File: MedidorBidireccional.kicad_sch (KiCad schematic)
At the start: 28 parts, among them J1 ADC conector, J2 Pickit, U1 RN4870-I_RM140, U2 47L04-E_ST, U3 25AA320A-I_ST, U4 PIC24FJ128GA310-I_PT

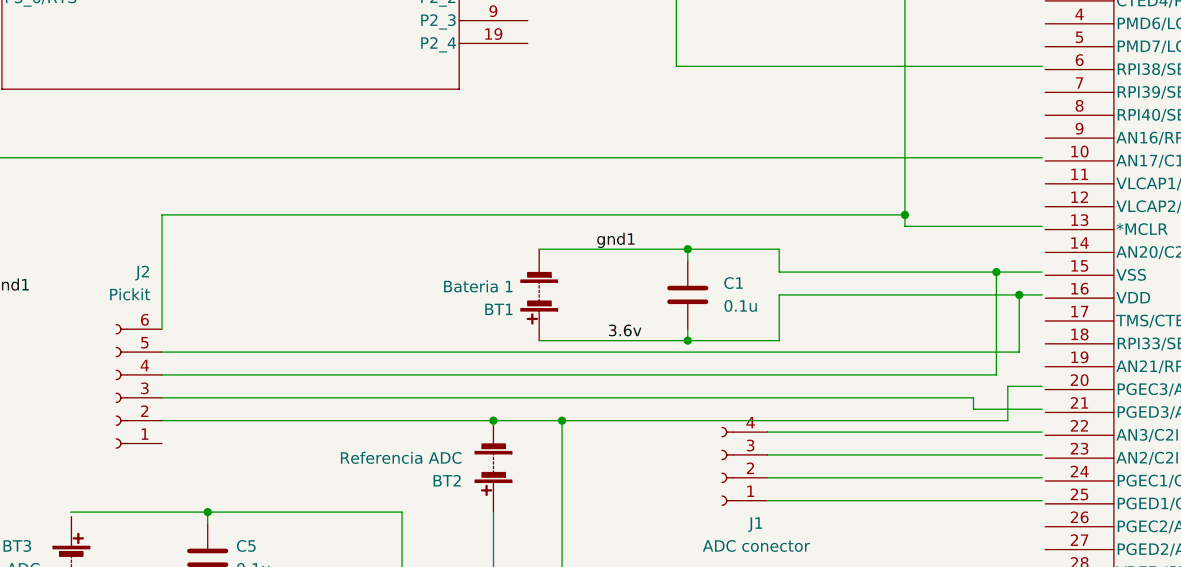
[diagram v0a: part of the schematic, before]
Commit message: se añade resistencia para pickit
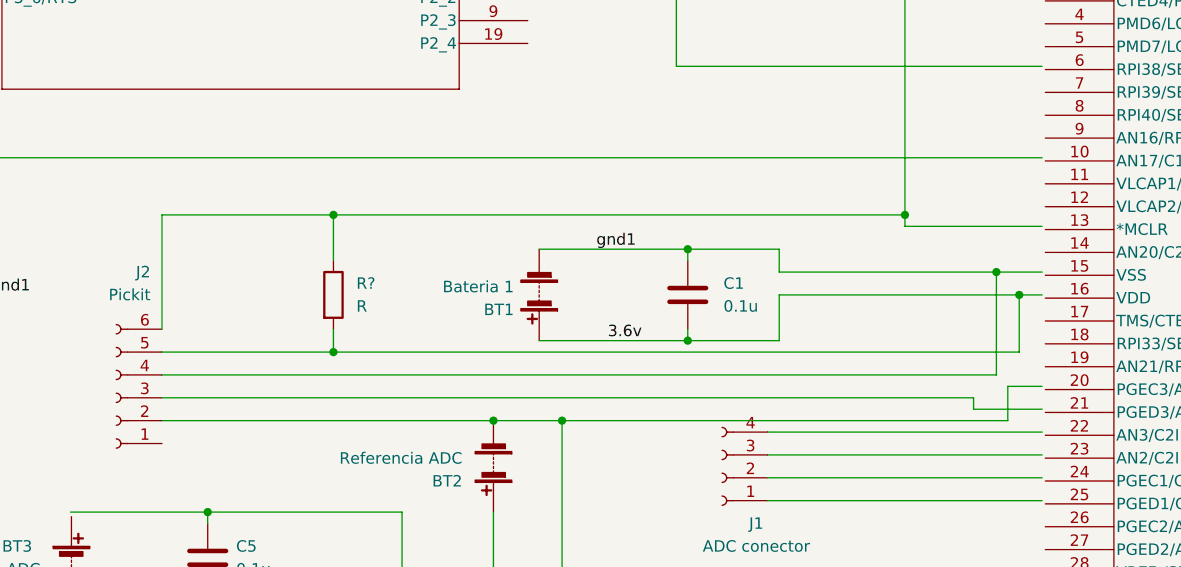
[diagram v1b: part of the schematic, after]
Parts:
- added R?: R, symbol Device:R
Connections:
- net 3.6v: now also R?.2
- net at J2.6 (Pin_6), R2.1: now also R?.1
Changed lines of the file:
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@@
   (junction (at 201.93 254) (diameter 0) (color 0 0 0 0)
   )
+  (junction (at 144.78 162.56) (diameter 0) (color 0 0 0 0)
+  )
   (junction (at 208.28 162.56) (diameter 0) (color 0 0 0 0)
   )
@@
   )
   (junction (at 198.12 226.06) (diameter 0) (color 0 0 0 0)
+  )
+  (junction (at 144.78 177.8) (diameter 0) (color 0 0 0 0)
   )
   (junction (at 170.18 185.42) (diameter 0) (color 0 0 0 0)
@@
     (stroke (width 0) (type default) (color 0 0 0 0))
   )
+  (wire (pts (xy 144.78 177.8) (xy 220.98 177.8))
+    (stroke (width 0) (type default) (color 0 0 0 0))
+  )
   (wire (pts (xy 467.36 82.55) (xy 538.48 82.55))
     (stroke (width 0) (type default) (color 0 0 0 0))
@@
     (stroke (width 0) (type default) (color 0 0 0 0))
   )
+  (wire (pts (xy 144.78 175.26) (xy 144.78 177.8))
+    (stroke (width 0) (type default) (color 0 0 0 0))
+  )
   (wire (pts (xy 220.98 171.45) (xy 223.52 171.45))
     (stroke (width 0) (type default) (color 0 0 0 0))
@@
     (stroke (width 0) (type default) (color 0 0 0 0))
   )
-  (wire (pts (xy 125.73 162.56) (xy 208.28 162.56))
+  (wire (pts (xy 125.73 162.56) (xy 144.78 162.56))
     (stroke (width 0) (type default) (color 0 0 0 0))
   )
@@
     (stroke (width 0) (type default) (color 0 0 0 0))
   )
-  (wire (pts (xy 125.73 177.8) (xy 220.98 177.8))
+  (wire (pts (xy 125.73 177.8) (xy 144.78 177.8))
     (stroke (width 0) (type default) (color 0 0 0 0))
   )
@@
     (stroke (width 0) (type default) (color 0 0 0 0))
   )
+  (wire (pts (xy 144.78 162.56) (xy 208.28 162.56))
+    (stroke (width 0) (type default) (color 0 0 0 0))
+  )
   (wire (pts (xy 480.06 97.79) (xy 525.78 97.79))
     (stroke (width 0) (type default) (color 0 0 0 0))
@@
   )
   (wire (pts (xy 431.8 194.31) (xy 482.6 194.31))
+    (stroke (width 0) (type default) (color 0 0 0 0))
+  )
+  (wire (pts (xy 144.78 162.56) (xy 144.78 167.64))
     (stroke (width 0) (type default) (color 0 0 0 0))
   )
@@
     (pin "9")
   )
+  (symbol (lib_id "Device:R") (at 144.78 171.45 0) (unit 1)
+    (in_bom yes) (on_board yes) (fields_autoplaced)
+    (property "Reference" "R?" (id 0) (at 147.32 170.1799 0)
+      (effects (font (size 1.27 1.27)) (justify left))
+    )
+    (property "Value" "R" (id 1) (at 147.32 172.7199 0)
+      (effects (font (size 1.27 1.27)) (justify left))
+    )
+    (property "Footprint" "" (id 2) (at 143.002 171.45 90)
+      (effects (font (size 1.27 1.27)) hide)
+    )
+    (property "Datasheet" "~" (id 3) (at 144.78 171.45 0)
+      (effects (font (size 1.27 1.27)) hide)
+    )
+    (pin "1")
+    (pin "2")
+  )
   (symbol (lib_id "Connector:Conn_01x18_Female") (at 523.24 120.65 90) (unit 1)
     (in_bom yes) (on_board yes)
@@
       (reference "R6") (unit 1) (value "330") (footprint "")
     )
+    (path "/7cf4a546-1a3b-444f-85e5-1343f72e38f0"
+      (reference "R?") (unit 1) (value "R") (footprint "")
+    )
     (path "/9b2818c2-72ef-4d3f-9cc7-e18b19154a65"

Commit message: se actualiza circuito de conector de pickit
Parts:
- added C10: 10uF, symbol Device:C
- added J3, J4: Jp, symbol Connector:Conn_01x01_Female
- C6: value C -> 6.8uF
- R7: renamed from R?; value R -> 10K
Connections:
- net gnd1: now also C10.2
- net at J2.6 (Pin_6), R7.1: now also J4.1 (Pin_1); no longer R2.1
- new net: J3.1 (Pin_1), R2.1
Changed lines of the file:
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@@
   (junction (at 201.93 254) (diameter 0) (color 0 0 0 0)
   )
+  (junction (at 208.28 162.56) (diameter 0) (color 0 0 0 0)
+  )
   (junction (at 144.78 162.56) (diameter 0) (color 0 0 0 0)
   )
-  (junction (at 208.28 162.56) (diameter 0) (color 0 0 0 0)
-  )
   (junction (at 35.56 120.65) (diameter 0) (color 0 0 0 0)
   )
@@
   )
   (junction (at 130.81 205.74) (diameter 0) (color 0 0 0 0)
+  )
+  (junction (at 494.03 196.85) (diameter 0) (color 0 0 0 0)
   )
   (no_connect (at 515.62 110.49))
@@
     (stroke (width 0) (type default) (color 0 0 0 0))
   )
+  (wire (pts (xy 494.03 182.88) (xy 494.03 196.85))
+    (stroke (width 0) (type default) (color 0 0 0 0))
+  )
   (wire (pts (xy 535.94 125.73) (xy 535.94 158.75))
     (stroke (width 0) (type default) (color 0 0 0 0))
@@
     (stroke (width 0) (type default) (color 0 0 0 0))
   )
+  (wire (pts (xy 494.03 175.26) (xy 494.03 171.45))
+    (stroke (width 0) (type default) (color 0 0 0 0))
+  )
   (wire (pts (xy 208.28 240.03) (xy 223.52 240.03))
     (stroke (width 0) (type default) (color 0 0 0 0))
@@
     (stroke (width 0) (type default) (color 0 0 0 0))
   )
+  (wire (pts (xy 431.8 171.45) (xy 494.03 171.45))
+    (stroke (width 0) (type default) (color 0 0 0 0))
+  )
   (wire (pts (xy 431.8 191.77) (xy 480.06 191.77))
     (stroke (width 0) (type default) (color 0 0 0 0))
@@
     (stroke (width 0) (type default) (color 0 0 0 0))
   )
-  (wire (pts (xy 208.28 123.19) (xy 208.28 162.56))
-    (stroke (width 0) (type default) (color 0 0 0 0))
-  )
   (wire (pts (xy 485.14 207.01) (xy 485.14 101.6))
     (stroke (width 0) (type default) (color 0 0 0 0))
@@
     (stroke (width 0) (type default) (color 0 0 0 0))
   )
+  (wire (pts (xy 208.28 139.7) (xy 208.28 162.56))
+    (stroke (width 0) (type default) (color 0 0 0 0))
+  )
   (wire (pts (xy 182.88 110.49) (xy 182.88 146.05))
     (stroke (width 0) (type default) (color 0 0 0 0))
@@
     (stroke (width 0) (type default) (color 0 0 0 0))
   )
+  (wire (pts (xy 494.03 196.85) (xy 524.51 196.85))
+    (stroke (width 0) (type default) (color 0 0 0 0))
+  )
   (wire (pts (xy 440.69 231.14) (xy 431.8 231.14))
     (stroke (width 0) (type default) (color 0 0 0 0))
@@
     (stroke (width 0) (type default) (color 0 0 0 0))
   )
-  (wire (pts (xy 441.96 196.85) (xy 524.51 196.85))
+  (wire (pts (xy 441.96 196.85) (xy 494.03 196.85))
     (stroke (width 0) (type default) (color 0 0 0 0))
   )
@@
     (stroke (width 0) (type default) (color 0 0 0 0))
   )
+  (wire (pts (xy 208.28 123.19) (xy 208.28 133.35))
+    (stroke (width 0) (type default) (color 0 0 0 0))
+  )
   (wire (pts (xy 130.81 195.58) (xy 152.4 195.58))
     (stroke (width 0) (type default) (color 0 0 0 0))
@@
   )
   (wire (pts (xy 193.04 254) (xy 201.93 254))
+    (stroke (width 0) (type default) (color 0 0 0 0))
+  )
+  (wire (pts (xy 205.74 133.35) (xy 208.28 133.35))
     (stroke (width 0) (type default) (color 0 0 0 0))
   )
@@
     (pin "2")
   )
+  (symbol (lib_id "Device:C") (at 494.03 179.07 0) (unit 1)
+    (in_bom yes) (on_board yes) (fields_autoplaced)
+    (property "Reference" "C10" (id 0) (at 497.84 177.7999 0)
+      (effects (font (size 1.27 1.27)) (justify left))
+    )
+    (property "Value" "10uF" (id 1) (at 497.84 180.3399 0)
+      (effects (font (size 1.27 1.27)) (justify left))
+    )
+    (property "Footprint" "" (id 2) (at 494.9952 182.88 0)
+      (effects (font (size 1.27 1.27)) hide)
+    )
+    (property "Datasheet" "~" (id 3) (at 494.03 179.07 0)
+      (effects (font (size 1.27 1.27)) hide)
+    )
+    (pin "1")
+    (pin "2")
+  )
   (symbol (lib_id "Device:Battery") (at 524.51 176.53 0) (unit 1)
     (in_bom yes) (on_board yes) (fields_autoplaced)
@@
     (pin "1")
     (pin "2")
+  )
+  (symbol (lib_id "Connector:Conn_01x01_Female") (at 200.66 133.35 180) (unit 1)
+    (in_bom yes) (on_board yes) (fields_autoplaced)
+    (property "Reference" "J3" (id 0) (at 201.295 128.27 0))
+    (property "Value" "Jp" (id 1) (at 201.295 130.81 0))
+    (property "Footprint" "" (id 2) (at 200.66 133.35 0)
+      (effects (font (size 1.27 1.27)) hide)
+    )
+    (property "Datasheet" "~" (id 3) (at 200.66 133.35 0)
+      (effects (font (size 1.27 1.27)) hide)
+    )
+    (pin "1")
   )
   (symbol (lib_id "2023-05-13_06-14-04:25AA320A-I_ST") (at 160.02 242.57 180) (unit 1)
@@
   (symbol (lib_id "Device:R") (at 144.78 171.45 0) (unit 1)
     (in_bom yes) (on_board yes) (fields_autoplaced)
-    (property "Reference" "R?" (id 0) (at 147.32 170.1799 0)
-      (effects (font (size 1.27 1.27)) (justify left))
-    )
-    (property "Value" "R" (id 1) (at 147.32 172.7199 0)
+    (property "Reference" "R7" (id 0) (at 147.32 170.1799 0)
+      (effects (font (size 1.27 1.27)) (justify left))
+    )
+    (property "Value" "10K" (id 1) (at 147.32 172.7199 0)
       (effects (font (size 1.27 1.27)) (justify left))
     )
@@
     (pin "2")
   )
+  (symbol (lib_id "Connector:Conn_01x01_Female") (at 203.2 139.7 180) (unit 1)
+    (in_bom yes) (on_board yes)
+    (property "Reference" "J4" (id 0) (at 200.66 139.7 0))
+    (property "Value" "Jp" (id 1) (at 200.66 142.24 0))
+    (property "Footprint" "" (id 2) (at 203.2 139.7 0)
+      (effects (font (size 1.27 1.27)) hide)
+    )
+    (property "Datasheet" "~" (id 3) (at 203.2 139.7 0)
+      (effects (font (size 1.27 1.27)) hide)
+    )
+    (pin "1")
+  )
   (symbol (lib_id "Device:R") (at 208.28 99.06 0) (unit 1)
     (in_bom yes) (on_board yes) (fields_autoplaced)
@@
       (effects (font (size 1.27 1.27)) (justify left))
     )
-    (property "Value" "C" (id 1) (at 471.17 259.0799 0)
+    (property "Value" "6.8uF" (id 1) (at 471.17 259.0799 0)
       (effects (font (size 1.27 1.27)) (justify left))
     )
@@
     )
     (path "/fa281287-10b3-4de3-a84a-0705647d3d24"
-      (reference "C6") (unit 1) (value "C") (footprint "")
+      (reference "C6") (unit 1) (value "6.8uF") (footprint "")
     )
     (path "/8828fd7c-88d5-4718-964e-3d22b4e00f40"
@@
       (reference "C9") (unit 1) (value "0.1u") (footprint "")
     )
+    (path "/2fa991c7-7026-4091-9c19-bb88e45d34cc"
+      (reference "C10") (unit 1) (value "10uF") (footprint "")
+    )
     (path "/dc15c646-f12d-437b-afc7-c556c6a4b54b"
       (reference "D1") (unit 1) (value "LED") (footprint "")
@@
       (reference "J2") (unit 1) (value "Pickit") (footprint "")
     )
+    (path "/5a297127-831a-431d-b3ee-e398d843195e"
+      (reference "J3") (unit 1) (value "Jp") (footprint "")
+    )
+    (path "/c44b31cd-24b9-4130-89c9-6dacb216899c"
+      (reference "J4") (unit 1) (value "Jp") (footprint "")
+    )
     (path "/816aa873-1c95-426e-97ce-2738bfc218ea"
       (reference "LCD1") (unit 1) (value "Conn_01x18_Female") (footprint "")
@@
     )
     (path "/7cf4a546-1a3b-444f-85e5-1343f72e38f0"
-      (reference "R?") (unit 1) (value "R") (footprint "")
+      (reference "R7") (unit 1) (value "10K") (footprint "")
     )
     (path "/9b2818c2-72ef-4d3f-9cc7-e18b19154a65"

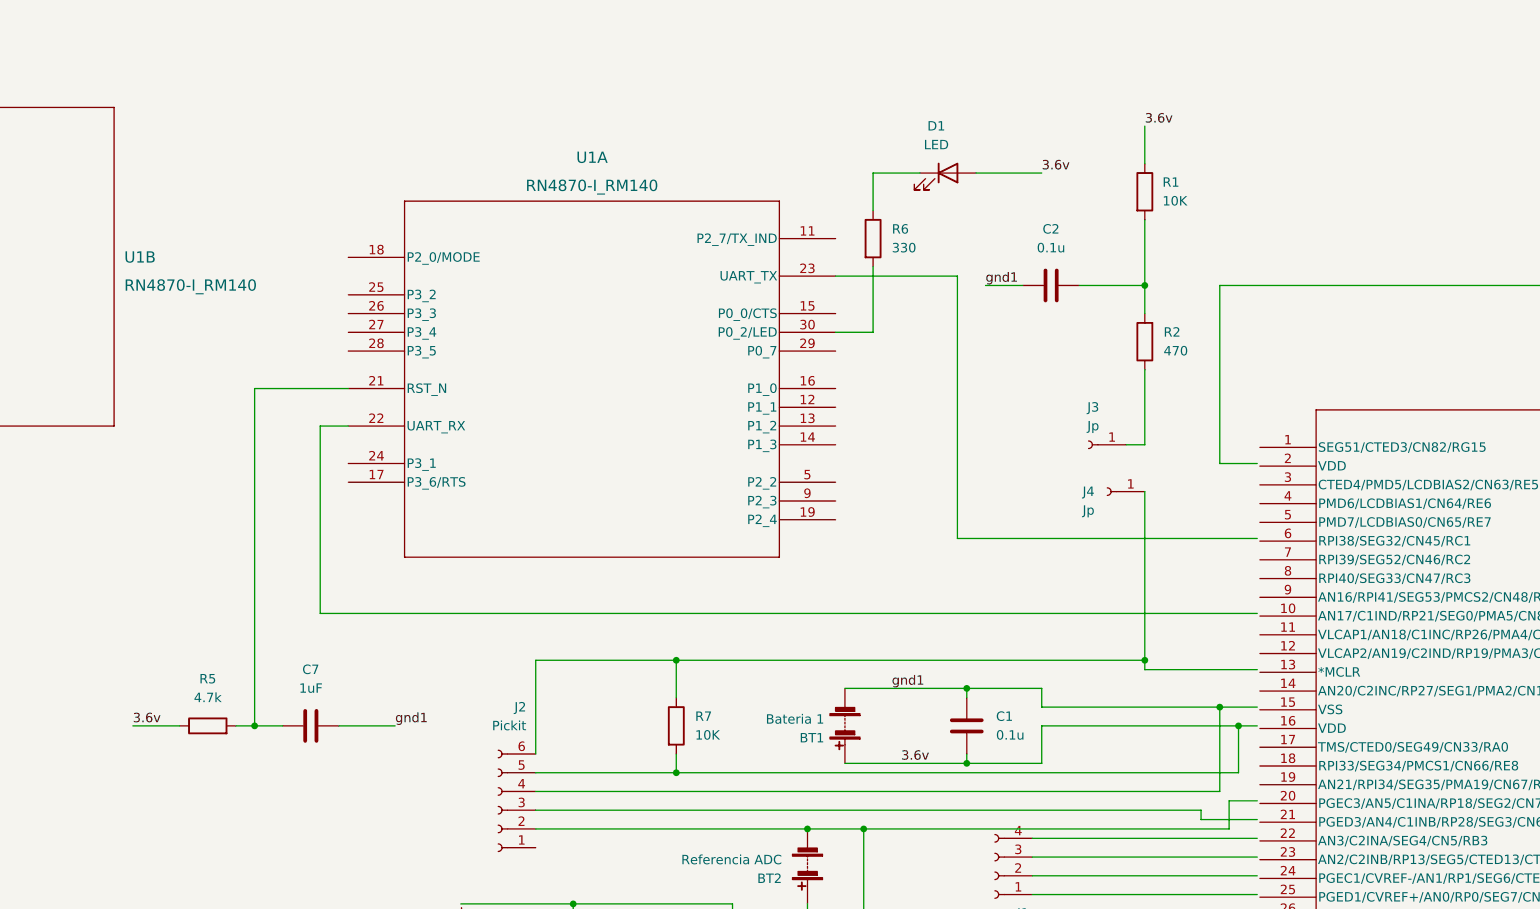
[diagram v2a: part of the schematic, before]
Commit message: se quita conecxion de pin rst en rn4870 y se agrega conector para jumper en mclr de pic
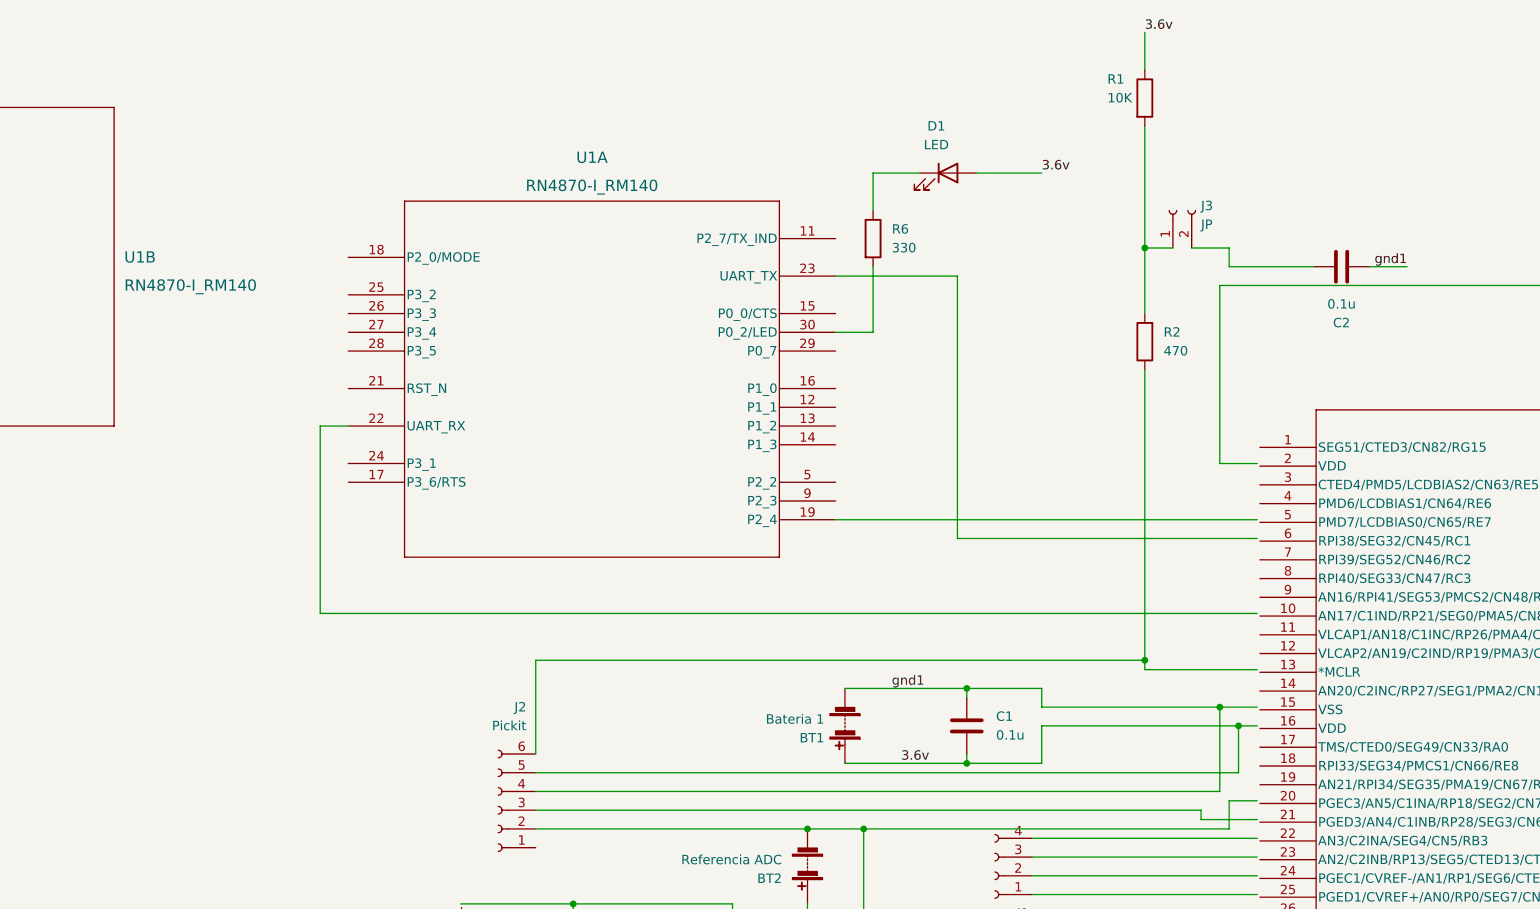
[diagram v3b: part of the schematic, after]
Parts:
- removed C7: 1uF, symbol Device:C
- removed J3, J4: Jp, symbol Connector:Conn_01x01_Female
- removed R5: 4.7k, symbol Device:R
- removed R7: 10K, symbol Device:R
- added J3: JP, symbol Connector:Conn_01x02_Female
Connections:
- net at J2.6 (Pin_6): now also R2.1
- net at R1.2, R2.2: now also J3.1 (Pin_1); no longer C2.1
- new net: C2.1, J3.2 (Pin_2)
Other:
- moved on the sheet: C2, R1
